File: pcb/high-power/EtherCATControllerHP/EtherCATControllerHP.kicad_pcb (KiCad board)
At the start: 6 copper layers, 76 x 76 mm, 186 parts, among them J1 DNP, J2 Right Angle 1x4, J3 Conn_01x04_Socket, J4 TYPE-C-31-M-12, J5 XT60PW-M, J6 2 pin Molex Picoblade, J7 DEBUG POWER, SW1 EVP-AA202K, U1 STM32F405RGT6, U2 TPS54360DDAR, U3 LDL1117S33R, U4 LAN9252I/ML, U5 AS5047P-ATSM, U6 MCF8329A1IREER, U7 24FC512-I/SN, U8 SN65HVD231, Y1 ABM3B-8.000MHZ-10-1-U-T, Y2 ABM8-25.000MHZ-D2Y-T

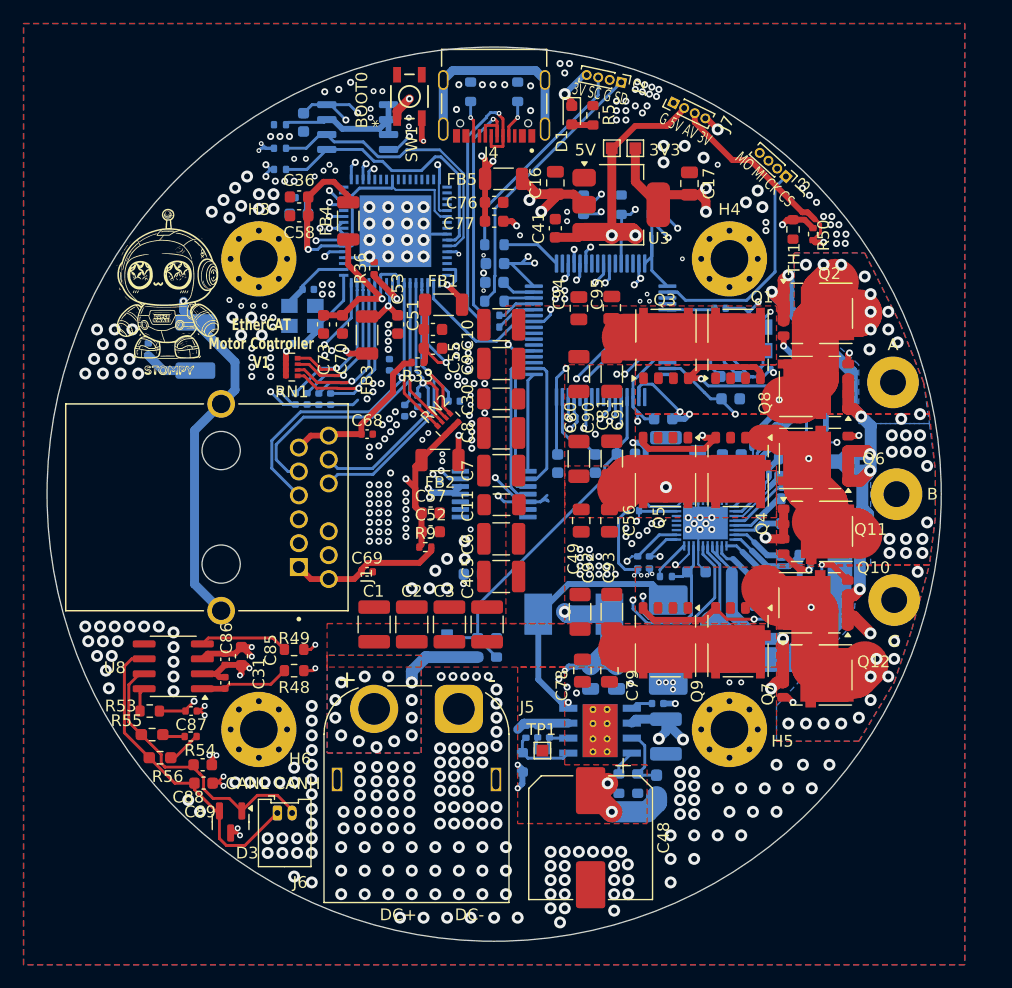
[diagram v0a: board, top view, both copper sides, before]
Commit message: redid layout and mounting
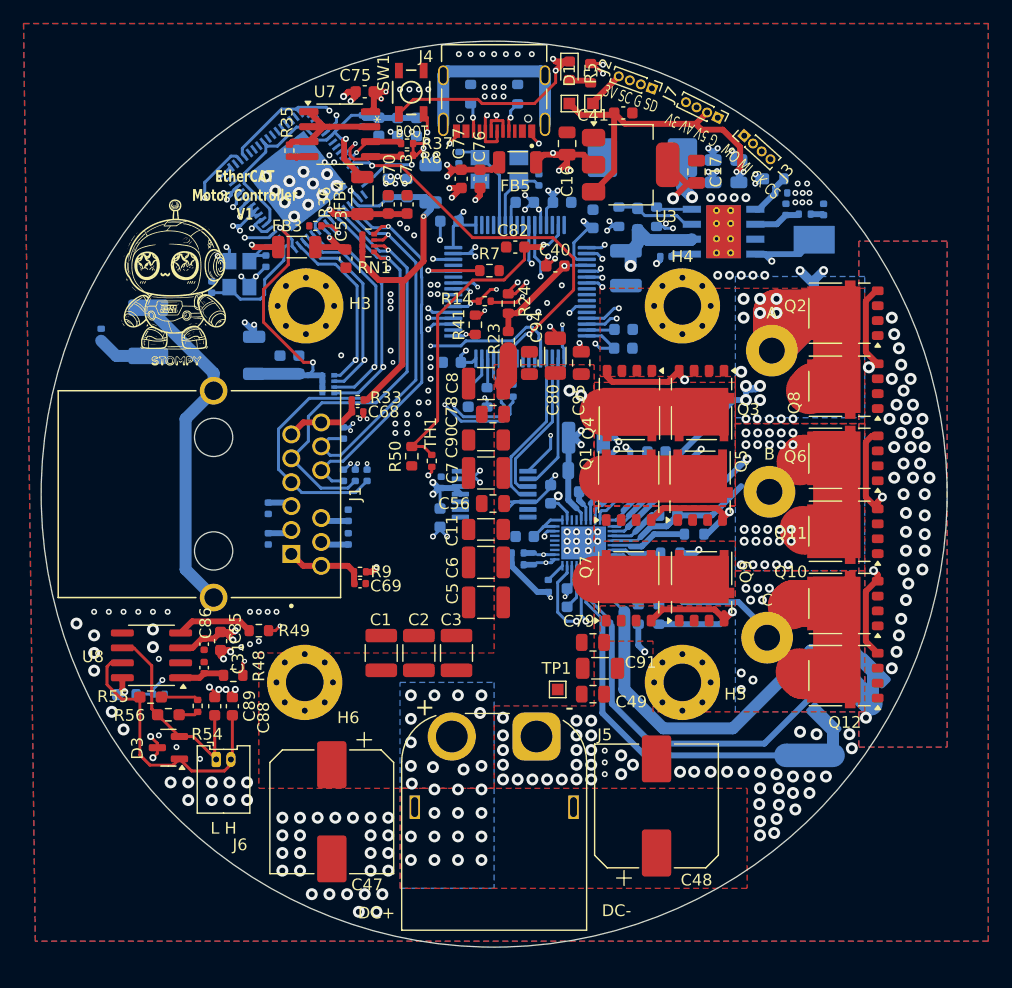
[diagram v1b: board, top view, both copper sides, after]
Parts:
- removed C10, C4, C9: 10uF, Capacitor_SMD:C_1210_3225Metric
- removed C30, C81, C92, C93: 1uF, Capacitor_SMD:C_1206_3216Metric
- removed TP4: TESTPOINT, TestPoint:TestPoint_Pad_1.0x1.0mm
- added C47: 100uF, 80V, Capacitor_SMD:CP_Elec_10x10, F.Cu at (136.2, 127.0)
- added NT1: NetTie_2, NetTie:NetTie-2_SMD_Pad2.0mm, B.Cu at (176.8, 122.2)
- added NT2: NetTie_2, NetTie:NetTie-2_SMD_Pad2.0mm, B.Cu at (180.6, 116.4)
- C36, C51, C52, C55, C57, C58, C87, FB1, FB2, R53, RN2: moved to B.Cu
- C40, C75, C82, R14, R23, R24, R35, R37, R41, R7, R8, U7: moved to F.Cu
- moved R38 54.0 mm to (173.8, 73.2), turned to 0 degrees
- moved R4 50.8 mm to (176.4, 76.2), turned to 0 degrees
- moved R39 50.7 mm to (174.4, 74.4), turned to 0 degrees
- moved C15 50.6 mm to (178.0, 75.8)
- moved C18 48.7 mm to (174.8, 75.8)
- moved R1 48.3 mm to (163.8, 76.4)
- moved R2 48.2 mm to (162.2, 76.6)
- moved R3 48.2 mm to (160.6, 76.4)
- moved C72 44.9 mm to (170.8, 72.5), turned to 90 degrees
- moved C74 43.8 mm to (168.6, 72.5), turned to 90 degrees
- moved U2 43.7 mm to (169.5, 77.7), turned to 0 degrees
- moved D2 41.1 mm to (162.6, 71.4), turned to 180 degrees
- moved C12 39.9 mm to (161.2, 80.8)
- moved C14 38.0 mm to (164.6, 79.8), turned to 180 degrees
- moved R50 37.7 mm to (143.0, 96.8)
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- renumbered 3V3 to TP2, 5V to TP3
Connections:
- J1 pad 10: /ETH1_TXN -> /ETH0_TXN
- J1 pad 11: /ETH1_TXP -> /ETH0_TXP
- J1 pad 2: /ETH0_TXN -> /ETH1_TXN
- J1 pad 3: /ETH0_TXP -> /ETH1_TXP
- J1 pad 4: /ETH1_RXP -> /ETH0_RXP
- J1 pad 5: /ETH1_RXN -> /ETH0_RXN
- J1 pad 8: /ETH0_RXP -> /ETH1_RXP
- J1 pad 9: /ETH0_RXN -> /ETH1_RXN
- Q10 pad 1: /Motor/SENSE_P -> /Motor/LSS
- Q10 pad 2: /Motor/SENSE_P -> /Motor/LSS
- Q10 pad 3: /Motor/SENSE_P -> /Motor/LSS
- Q11 pad 1: /Motor/SENSE_P -> /Motor/LSS
- Q11 pad 2: /Motor/SENSE_P -> /Motor/LSS
- Q11 pad 3: /Motor/SENSE_P -> /Motor/LSS
- Q12 pad 1: /Motor/SENSE_P -> /Motor/LSS
- Q12 pad 2: /Motor/SENSE_P -> /Motor/LSS
- Q12 pad 3: /Motor/SENSE_P -> /Motor/LSS
- Q2 pad 1: /Motor/SENSE_P -> /Motor/LSS
- Q2 pad 2: /Motor/SENSE_P -> /Motor/LSS
- Q2 pad 3: /Motor/SENSE_P -> /Motor/LSS
- Q6 pad 1: /Motor/SENSE_P -> /Motor/LSS
- Q6 pad 2: /Motor/SENSE_P -> /Motor/LSS
- Q6 pad 3: /Motor/SENSE_P -> /Motor/LSS
- Q8 pad 1: /Motor/SENSE_P -> /Motor/LSS
- Q8 pad 2: /Motor/SENSE_P -> /Motor/LSS
- Q8 pad 3: /Motor/SENSE_P -> /Motor/LSS
- R12 pad 1: VCC -> AVCC
- R13 pad 1: VCC -> AVCC
- R6 pad 1: /Motor/SENSE_P -> /Motor/LSS
- U1 pad 17: unconnected-(U1-PA3-Pad17) -> /SPI_CS
- U1 pad 2: /SPI_CS -> unconnected-(U1-PC13-Pad2)
- U1 pad 43: /SPI2_CS -> unconnected-(U1-PA10-Pad43)
- U1 pad 62: unconnected-(U1-PB9-Pad62) -> /SPI2_CS
- U4 pad 52: /ETH1_TXN -> /ETH0_TXN
- U4 pad 53: /ETH1_TXP -> /ETH0_TXP
- U4 pad 54: /ETH1_RXN -> /ETH0_RXN
- U4 pad 55: /ETH1_RXP -> /ETH0_RXP
- U4 pad 60: /ETH0_RXP -> /ETH1_RXP
- U4 pad 61: /ETH0_RXN -> /ETH1_RXN
- U4 pad 62: /ETH0_TXP -> /ETH1_TXP
- U4 pad 63: /ETH0_TXN -> /ETH1_TXN
- U6 pad 21: /Motor/SENSE_P -> /Motor/LSS
- U6 pad 23: GND -> /Motor/SENSE_N
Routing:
- net /Motor/SENSE_P: track 113.9 -> 35.6 mm, vias 10 -> 0
- net 5V: track 103.5 -> 40.6 mm, vias 6 -> 8
- net AVCC: track 122.1 -> 81.0 mm
- net /Motor/LSS: track 0.00 -> 40.4 mm, vias 0 -> 39
- net GND: track 121.6 -> 88.0 mm, vias 472 -> 277
- net /Motor/SENSE_N: track 0.00 -> 30.2 mm
- net /VBUS_SENSE: track 30.8 -> 9.91 mm, vias 0 -> 1
- net /ETHRST: track 28.0 -> 47.9 mm
- net /IRQ: track 14.0 -> 33.3 mm
- net /EtherCAT/I2C_SCL: track 24.6 -> 5.31 mm, vias 0 -> 1
- net /USB_D+: track 22.4 -> 38.8 mm, vias 1 -> 2
- net /EtherCAT/I2C_SDA: track 23.6 -> 7.28 mm, vias 0 -> 1
- net VCC: track 100.5 -> 84.2 mm, vias 21 -> 15
- net Net-(Q4-G): track 26.8 -> 11.1 mm, vias 2 -> 1
- net /SH_A: track 28.5 -> 41.7 mm, vias 14 -> 11
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- added copper zone on B.Cu, net /Motor/LSS
- added copper zone on F.Cu, net /Motor/LSS
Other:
- board size 76 x 76 mm -> 77 x 77 mm
- board text added: "BOOT"
- board text added: "L H"
- board text removed: "BOOT0"
- board text removed: "CANL CANH"

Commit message: production files
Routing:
- net GND: track 88.0 -> 129.5 mm, vias 277 -> 438
- net /SH_C: vias 8 -> 14
